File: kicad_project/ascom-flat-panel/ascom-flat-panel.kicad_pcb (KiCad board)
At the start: 4 copper layers, 55 x 29.5 mm, 14 parts, among them J1 Servo, J3 JST-XH LED, Q1 IRLZ34N, Q2 IRLZ34N, U1 XIAO-SAMD21-DIP

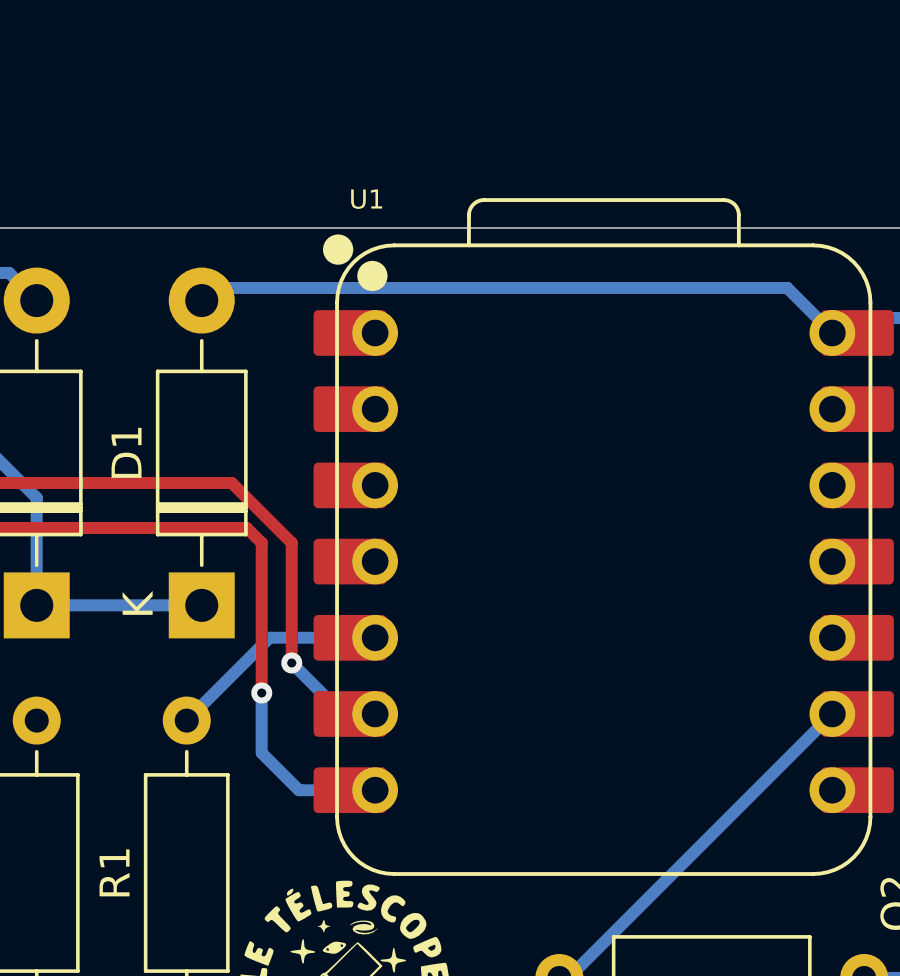
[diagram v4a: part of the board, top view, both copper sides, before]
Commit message: [kicad] - mise à jour valeur résistance 5k -> 4k7 suivant tests + ajustement de routage
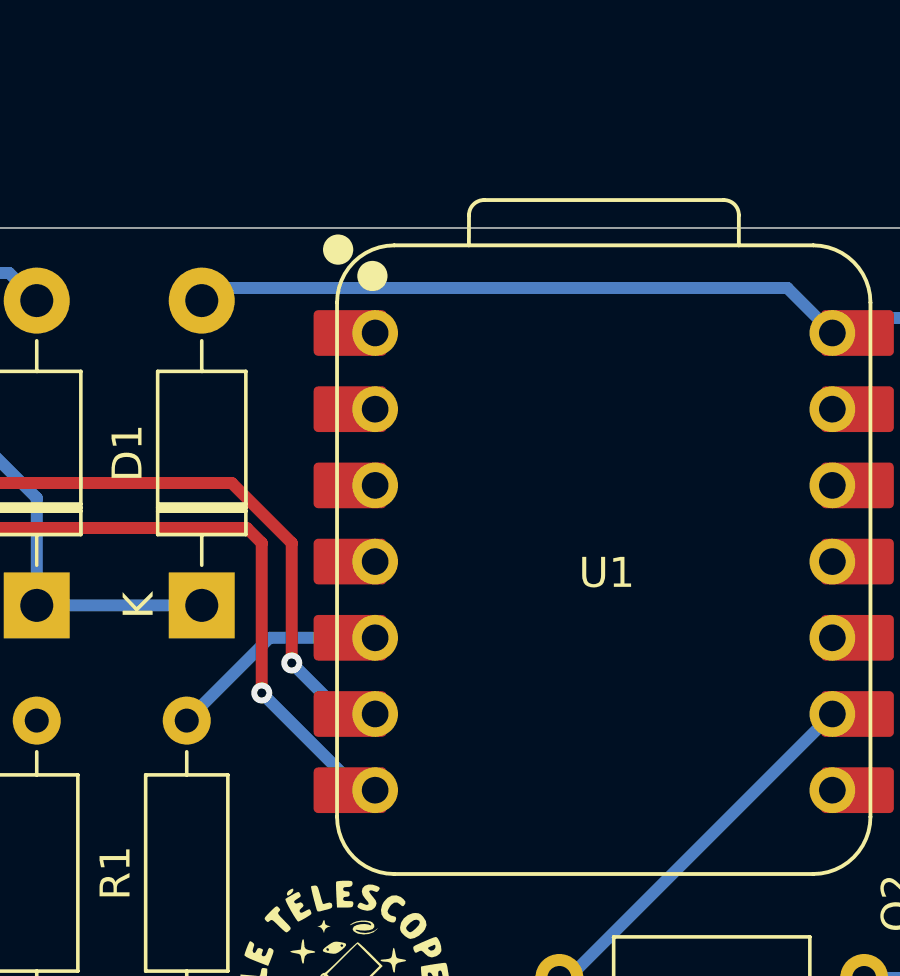
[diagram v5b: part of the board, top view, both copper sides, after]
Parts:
- R4: value 5kΩ -> 4.7kΩ
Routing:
- net SERVO POSITION FEEDBACK: track 24.9 -> 23.8 mm
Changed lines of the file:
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@@
 		(at 128 80.5575)
 		(property "Reference" "U1"
-			(at -8 -12 0)
+			(at 0 0.4425 0)
 			(unlocked yes)
 			(layer "F.SilkS")
 			(effects
 				(font
-					(size 0.635 0.635)
-					(thickness 0.1016)
+					(size 1 1)
+					(thickness 0.15)
 				)
 			)
@@
 			)
 		)
-		(property "Value" "5kΩ"
+		(property "Value" "4.7kΩ"
 			(at 5.08 2.37 90)
 			(layer "F.Fab")
@@
 	)
 	(segment
-		(start 116.5 85)
-		(end 116.5 87)
+		(start 119.74 88.24)
+		(end 116.5 85)
 		(width 0.4)
 		(layer "B.Cu")
@@
 	(segment
 		(start 120.28 88.24)
-		(end 117.74 88.24)
-		(width 0.4)
-		(layer "B.Cu")
-		(net 5)
-	)
-	(segment
-		(start 117.74 88.24)
-		(end 116.5 87)
+		(end 119.74 88.24)
 		(width 0.4)
 		(layer "B.Cu")

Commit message: [kicad] - renommage connecteur J3 -> J2
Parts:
- renumbered J3 to J2
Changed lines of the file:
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@@
 	(net 6 "SERVO POSITION CONTROL")
 	(net 7 "+3V3")
-	(net 8 "Net-(J3-Pin_2)")
+	(net 8 "Net-(J2-Pin_2)")
 	(net 9 "Net-(Q1-G)")
 	(net 10 "Net-(Q2-G)")
@@
 			(layers "*.Cu" "*.Mask")
 			(remove_unused_layers no)
-			(net 8 "Net-(J3-Pin_2)")
+			(net 8 "Net-(J2-Pin_2)")
 			(pinfunction "D")
 			(pintype "unspecified")
@@
 		(descr "JST XH series connector, B2B-XH-A (http://www.jst-mfg.com/product/pdf/eng/eXH.pdf), generated with kicad-footprint-generator")
 		(tags "connector JST XH vertical")
-		(property "Reference" "J3"
+		(property "Reference" "J2"
 			(at 1 4.5 180)
 			(layer "F.SilkS")
@@
 			(layer "F.Fab")
 		)
-		(fp_text user "${REFERENCE}"
-			(at 1.25 2.7 0)
-			(layer "F.Fab")
-			(effects
-				(font
-					(size 1 1)
-					(thickness 0.15)
-				)
-			)
-		)
 		(pad "1" thru_hole roundrect
 			(at 0 0)
@@
 			(layers "*.Cu" "*.Mask")
 			(remove_unused_layers no)
-			(net 8 "Net-(J3-Pin_2)")
+			(net 8 "Net-(J2-Pin_2)")
 			(pinfunction "Pin_2")
 			(pintype "passive")

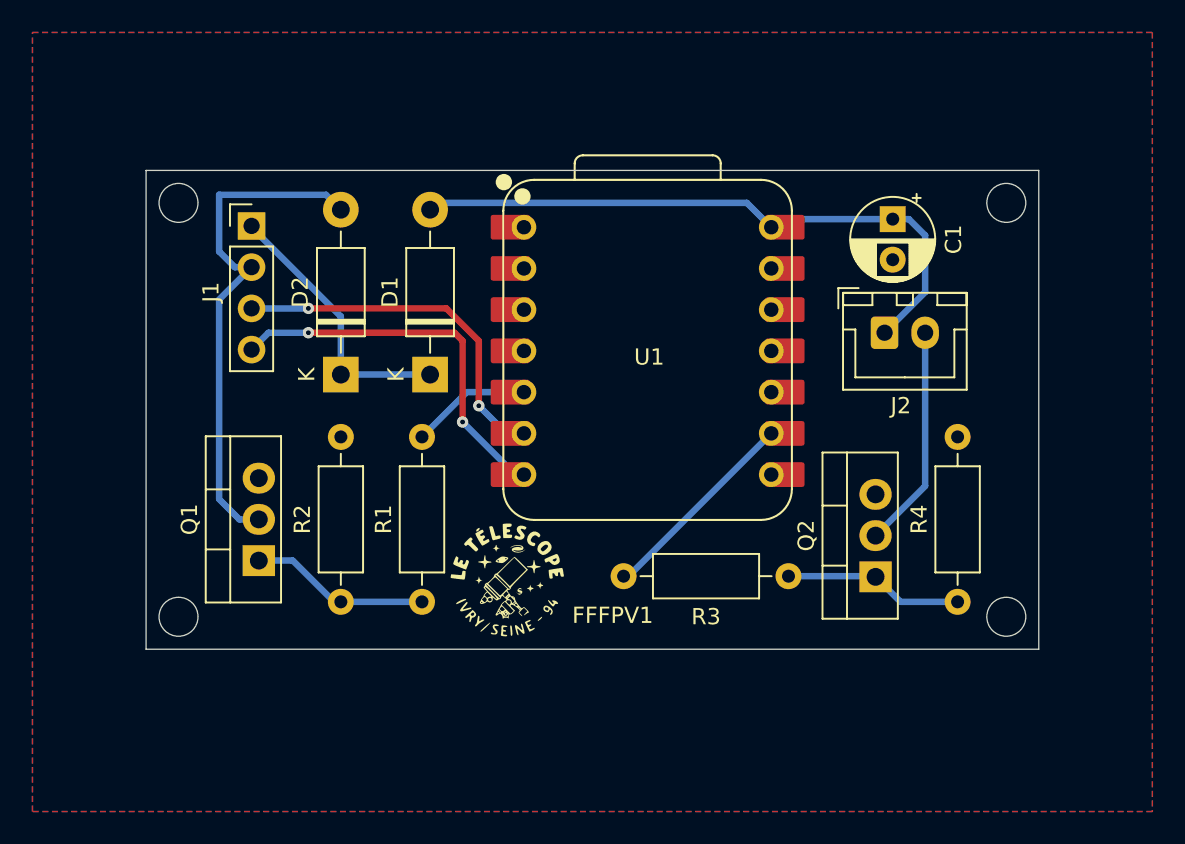
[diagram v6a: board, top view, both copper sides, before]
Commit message: [kicad] - Modification empreinte du Condensateur par cohérence avec les composants reçus (diam 6.3 au lieu de 5)
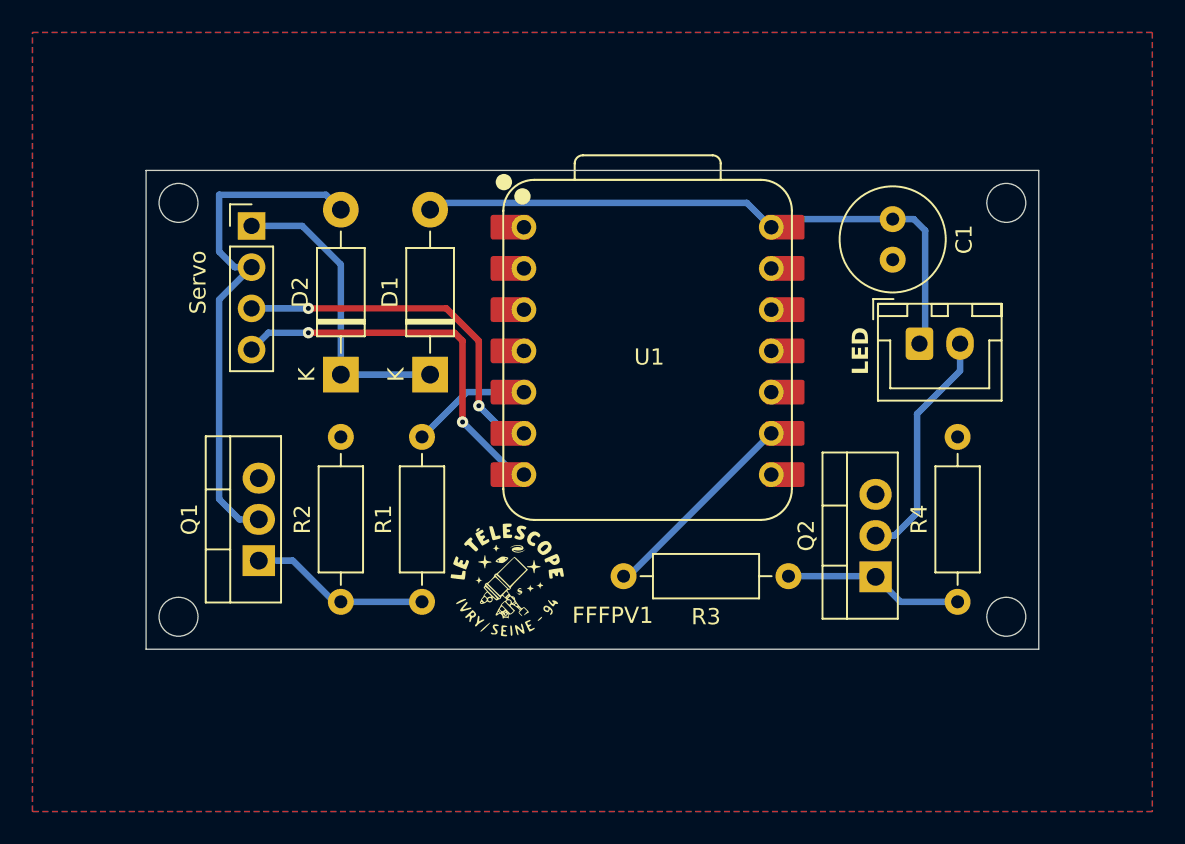
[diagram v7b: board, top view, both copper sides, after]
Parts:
- C1: footprint Capacitor_THT:CP_Radial_D5.0mm_P2.50mm -> Capacitor_THT:C_Radial_D6.3mm_H11.0mm_P2.50mm
- moved J2 2.25 mm to (144.7, 80.2)
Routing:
- net SERVO VCC: track 16.9 -> 18.8 mm
- net Net-(J2-Pin_2): track 13.8 -> 14.7 mm
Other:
- board text added: "LED"

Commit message: [kicad] - suppression du plan de masse de la couche supérieure de cuivre, a priori inutilisé
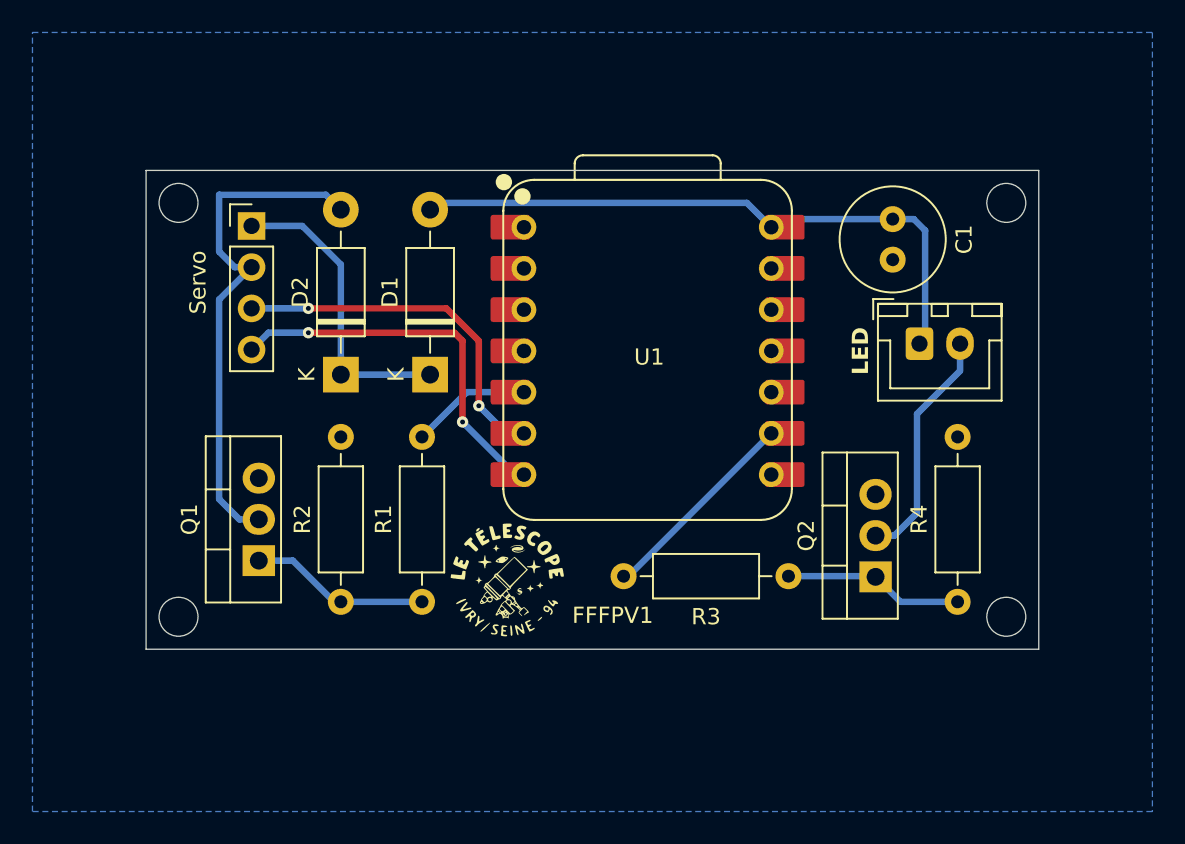
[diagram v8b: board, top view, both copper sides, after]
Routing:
- removed copper zone on F.Cu, net GND
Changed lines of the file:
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@@
 		(net 1)
 		(net_name "GND")
-		(layers "F.Cu" "B.Cu")
+		(layer "B.Cu")
 		(hatch edge 0.5)
 		(connect_pads
